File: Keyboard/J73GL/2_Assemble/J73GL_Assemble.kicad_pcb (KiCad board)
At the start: 2 copper layers, 305.2 x 99.2 mm, 224 parts, among them J1 Conn_01x02, SW1 SW_PUSH, SW10 SW_PUSH, SW11 SW_PUSH, SW12 SW_PUSH, SW13 SW_PUSH, SW14 SW_PUSH, SW15 SW_PUSH, SW16 SW_PUSH, SW17 SW_PUSH, SW18 SW_PUSH, SW19 SW_PUSH, SW2 SW_PUSH, SW20 SW_PUSH, SW21 SW_PUSH, SW22 SW_PUSH, SW23 SW_PUSH, SW24 SW_PUSH, SW25 SW_PUSH, SW26 SW_PUSH, SW27 SW_PUSH, SW28 SW_PUSH, SW29 SW_PUSH, SW3 SW_PUSH, SW30 SW_PUSH, SW31 SW_PUSH, SW32 SW_PUSH, SW33 SW_PUSH, SW34 SW_PUSH, SW35 SW_PUSH, SW36 SW_PUSH, SW37 SW_PUSH, SW38 SW_PUSH, SW39 SW_PUSH, SW4 SW_PUSH, SW40 SW_PUSH, SW41 SW_PUSH, SW42 SW_PUSH, SW43 SW_PUSH, SW44 SW_PUSH, SW45 SW_PUSH, SW46 SW_PUSH, SW47 SW_PUSH, SW48 SW_PUSH, SW49 SW_PUSH, SW5 SW_PUSH, SW50 SW_PUSH, SW51 SW_PUSH, SW52 SW_PUSH, SW53 SW_PUSH, SW54 SW_PUSH, SW55 SW_PUSH, SW56 SW_PUSH, SW57 SW_PUSH, SW58 SW_PUSH, SW59 SW_PUSH, SW6 SW_PUSH, SW60 SW_PUSH, SW61 SW_PUSH, SW62 SW_PUSH, SW63 SW_PUSH, SW64 SW_PUSH, SW65 SW_PUSH, SW66 SW_PUSH, SW67 SW_PUSH, SW68 SW_PUSH, SW69 SW_PUSH, SW7 SW_PUSH, SW70 SW_PUSH, SW71 SW_PUSH, SW72 SW_PUSH, SW73 SW_PUSH, SW74 SW_PUSH, SW75 KEY_SWITCH, SW8 SW_PUSH, SW9 SW_PUSH, U1 BLEMicroPro

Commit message: 寸法更新とか
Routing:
- net Col5: track 497.9 -> 495.3 mm
- net Net-(L63-Pad1): track 49.8 -> 48.2 mm
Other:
- board size 305.2 x 99.2 mm -> 304.4 x 98.8 mm
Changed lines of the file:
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@@
   (gr_line (start 264.325 17.55) (end 264.325 20.55) (layer F.Fab) (width 0.15))
   (gr_line (start 78.575 20.55) (end 264.325 20.55) (layer F.Fab) (width 0.15))
-  (gr_arc (start 320.825 20.05) (end 323.825 20.05) (angle -90) (layer Edge.Cuts) (width 0.1))
-  (gr_arc (start 320.825 113.25) (end 320.825 116.25) (angle -90) (layer Edge.Cuts) (width 0.1))
-  (gr_arc (start 21.575 20.05) (end 21.575 17.05) (angle -90) (layer Edge.Cuts) (width 0.1))
-  (gr_arc (start 21.575 113.25) (end 18.575 113.25) (angle -90) (layer Edge.Cuts) (width 0.1))
-  (gr_line (start 323.825 20.05) (end 323.825 113.25) (layer Edge.Cuts) (width 0.1))
-  (gr_line (start 18.575 20.05) (end 18.575 113.25) (layer Edge.Cuts) (width 0.1))
-  (gr_line (start 21.575 116.25) (end 320.825 116.25) (layer Edge.Cuts) (width 0.1))
-  (gr_line (start 320.825 17.05) (end 21.575 17.05) (layer Edge.Cuts) (width 0.1))
+  (gr_arc (start 320.625 20.25) (end 323.625 20.25) (angle -90) (layer Edge.Cuts) (width 0.1))
+  (gr_arc (start 320.625 113.05) (end 320.625 116.05) (angle -90) (layer Edge.Cuts) (width 0.1))
+  (gr_arc (start 22.275 20.25) (end 22.275 17.25) (angle -90) (layer Edge.Cuts) (width 0.1))
+  (gr_arc (start 22.275 113.05) (end 19.275 113.05) (angle -90) (layer Edge.Cuts) (width 0.1))
+  (gr_line (start 323.625 20.25) (end 323.625 113.05) (layer Edge.Cuts) (width 0.1))
+  (gr_line (start 19.275 20.25) (end 19.275 113.05) (layer Edge.Cuts) (width 0.1))
+  (gr_line (start 22.275 116.05) (end 320.625 116.05) (layer Edge.Cuts) (width 0.1))
+  (gr_line (start 320.625 17.25) (end 22.275 17.25) (layer Edge.Cuts) (width 0.1))
   (segment (start 38.1 22.2125) (end 36.05 24.2625) (width 0.25) (layer B.Cu) (net 1))
   (segment (start 38.1 22.0375) (end 38.1 22.2125) (width 0.25) (layer B.Cu) (net 1))
@@
   (segment (start 69.543205 70.093205) (end 70.025001 69.611409) (width 0.25) (layer F.Cu) (net 141))
   (segment (start 64.65 74.98641) (end 69.543205 70.093205) (width 0.25) (layer F.Cu) (net 141))
-  (via (at 68.3397 58.4) (size 0.8) (drill 0.4) (layers F.Cu B.Cu) (net 141))
-  (segment (start 70.025001 59.625001) (end 68.8 58.4) (width 0.25) (layer F.Cu) (net 141))
-  (segment (start 68.8 58.4) (end 68.3397 58.4) (width 0.25) (layer F.Cu) (net 141))
-  (segment (start 83.3 58.4) (end 68.3397 58.4) (width 0.25) (layer B.Cu) (net 141))
   (segment (start 84.4 59.5) (end 83.3 58.4) (width 0.25) (layer B.Cu) (net 141))
   (segment (start 84.4 60.85) (end 84.4 59.5) (width 0.25) (layer B.Cu) (net 141))
   (segment (start 84.0875 61.1625) (end 84.4 60.85) (width 0.25) (layer B.Cu) (net 141))
   (segment (start 83.4625 61.1625) (end 84.0875 61.1625) (width 0.25) (layer B.Cu) (net 141))
+  (segment (start 69.3 58.4) (end 69.28 58.38) (width 0.25) (layer B.Cu) (net 141))
+  (segment (start 72.24 58.4) (end 69.3 58.4) (width 0.25) (layer B.Cu) (net 141))
+  (via (at 69.28 58.38) (size 0.8) (drill 0.4) (layers F.Cu B.Cu) (net 141))
+  (segment (start 83.3 58.4) (end 72.24 58.4) (width 0.25) (layer B.Cu) (net 141))
+  (segment (start 70.025001 59.125001) (end 70.025001 59.625001) (width 0.25) (layer F.Cu) (net 141))
+  (segment (start 69.28 58.38) (end 70.025001 59.125001) (width 0.25) (layer F.Cu) (net 141))
   (via (at 61.774 57.9637) (size 0.8) (layers F.Cu B.Cu) (net 142))
   (via (at 50.75 43.6) (size 0.8) (drill 0.4) (layers F.Cu B.Cu) (net 142))
@@
   (segment (start 315.563 21.3114) (end 317.0516 22.8) (width 0.25) (layer F.Cu) (net 152))
   (segment (start 317.0516 22.8) (end 317.076601 22.774999) (width 0.25) (layer F.Cu) (net 152))
-  (segment (start 321.425001 22.774999) (end 322.5 21.7) (width 0.25) (layer F.Cu) (net 152))
-  (segment (start 322.5 21.7) (end 322.5 20.65) (width 0.25) (layer F.Cu) (net 152))
   (segment (start 321.598001 22.774999) (end 322.95 24.126998) (width 0.25) (layer F.Cu) (net 152))
   (segment (start 321.024999 22.774999) (end 321.598001 22.774999) (width 0.25) (layer F.Cu) (net 152))

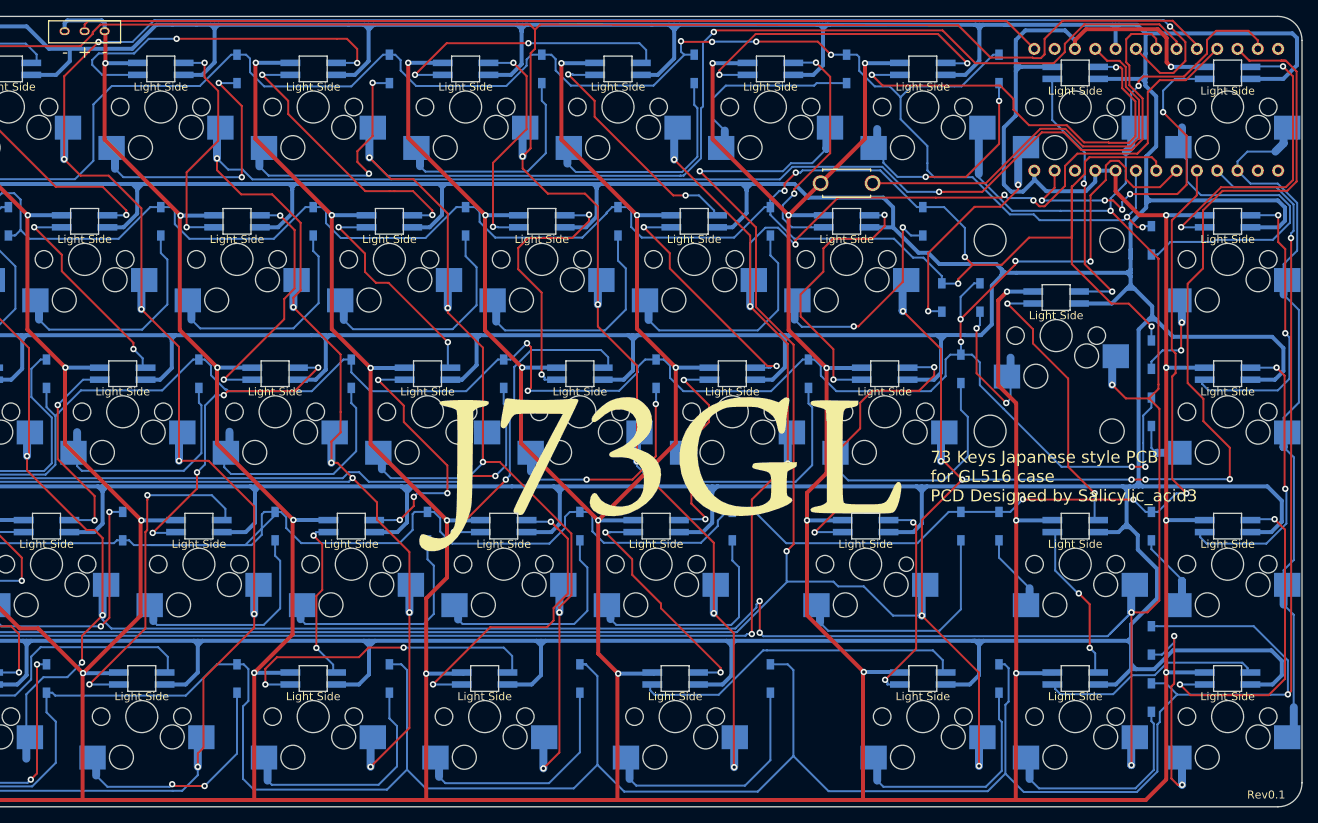
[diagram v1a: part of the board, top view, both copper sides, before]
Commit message: 電池コネクタの更新、シルクの修正
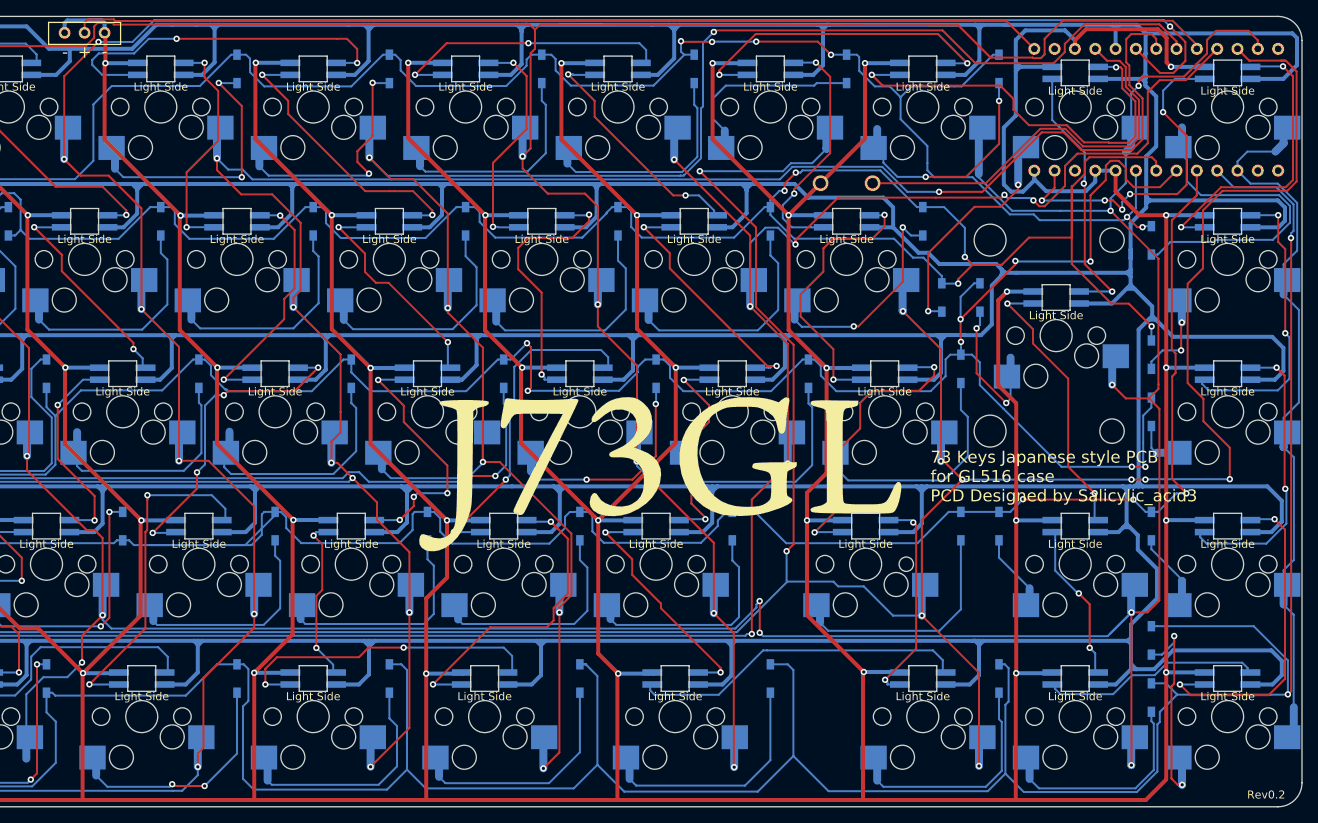
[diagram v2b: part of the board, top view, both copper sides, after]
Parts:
- J1: footprint kbd_Parts:Battery_XH2.5_GL_rev -> kbd_Parts:Battery_XH2.5_GL_PCB
- SW74: moved to F.Cu
- moved J1 0.20 mm to (171.4, 19.2)
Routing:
- net Col3: track 472.7 -> 473.6 mm
- net Bat+: track 121.2 -> 121.7 mm
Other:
- board text added: "Rev0.2"
- board text removed: "Rev0.1"

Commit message: シンボル、フットプリントの更新に合わせて更新
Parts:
- SW4: footprint kbd_SW:CherryMX_Hotswap_2u -> kbd_SW:CherryMX_Hotswap_2.25u
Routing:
- net Net-(L14-Pad1): track 27.6 -> 31.2 mm

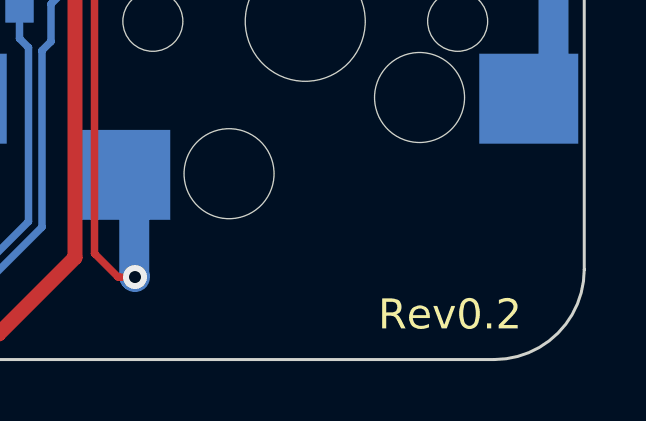
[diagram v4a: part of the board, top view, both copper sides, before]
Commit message: フットプリント名の変更に対応
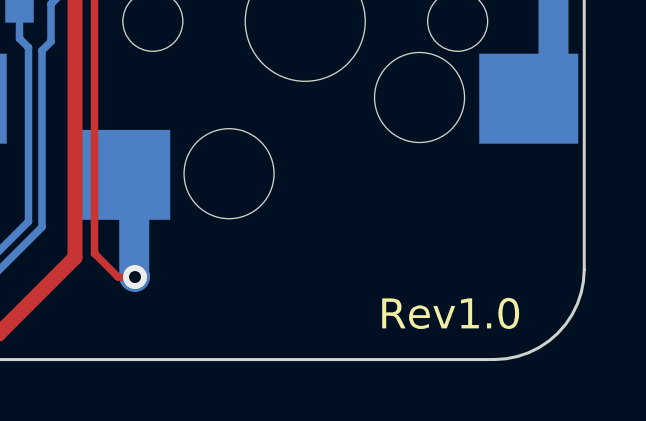
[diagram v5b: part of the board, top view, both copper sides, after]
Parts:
- SW1, SW10, SW11, SW12, SW13, SW14, SW16, SW17, SW18, SW19, SW20, SW21, SW22, SW23, SW24, SW26, SW27, SW28, SW29, SW30, SW31, SW32, SW33, SW34, SW35, SW36, SW37, SW38, SW39, SW41, SW42, SW43, SW44, SW45, SW46, SW47, SW48, SW49, SW51, SW52, SW53, SW54, SW56, SW57, SW58, SW59, SW6, SW60, SW61, SW63, SW64, SW66, SW67, SW68, SW7, SW70, SW71, SW72, SW73, SW8, SW9: footprint kbd_SW:CherryMX_Hotswap_1.0u -> kbd_SW:CherryMX_Hotswap_1u
- SW65, SW69: footprint kbd_SW:CherryMX_Hotswap_1.0u_Small1 -> kbd_SW:CherryMX_Hotswap_1u_Small1
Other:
- board text added: "Rev1.0"
- board text removed: "Rev0.2"
